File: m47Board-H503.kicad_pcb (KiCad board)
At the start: 4 copper layers, 40 x 34 mm, 42 parts, among them J1 USB_C_Receptacle_USB2.0_16P, J3 Conn_01x15_Pin, J4 Conn_01x10_Pin, J5 Conn_01x15_Pin, SW1 SW_Push, SW2 SW_Push, SW3 SW_Push, U1 AP2114H-3.3TRG1, U2 STM32H503CBTx, U3 USBLC6-2SC6, Y1 CX3225FB16000F0FZZH1 16MHz, Y2 ABS07-32.768KHZ-T

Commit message: Route tracks
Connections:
- J3 pad 14: Net-(J3-Pin_14) -> GND
- J3 pad 15: Net-(J3-Pin_15) -> +3.3V
- J4 pad 1: unconnected-(J4-Pin_1-Pad1) -> Net-(J4-Pin_1)
- J4 pad 10: unconnected-(J4-Pin_10-Pad10) -> /PA7
- J4 pad 2: unconnected-(J4-Pin_2-Pad2) -> Net-(J4-Pin_2)
- J4 pad 3: unconnected-(J4-Pin_3-Pad3) -> /PA0
- J4 pad 4: unconnected-(J4-Pin_4-Pad4) -> /PA1
- J4 pad 5: unconnected-(J4-Pin_5-Pad5) -> /PA2
- J4 pad 6: unconnected-(J4-Pin_6-Pad6) -> /PA3
- J4 pad 7: unconnected-(J4-Pin_7-Pad7) -> /PA4
- J4 pad 8: unconnected-(J4-Pin_8-Pad8) -> /PA5
- J4 pad 9: unconnected-(J4-Pin_9-Pad9) -> /PA6
- J5 pad 1: unconnected-(J5-Pin_1-Pad1) -> +3.3V
- J5 pad 10: unconnected-(J5-Pin_10-Pad10) -> /PB15
- J5 pad 11: unconnected-(J5-Pin_11-Pad11) -> /PA8
- J5 pad 12: unconnected-(J5-Pin_12-Pad12) -> /PA9
- J5 pad 13: unconnected-(J5-Pin_13-Pad13) -> /PA10
- J5 pad 14: unconnected-(J5-Pin_14-Pad14) -> GND
- J5 pad 15: unconnected-(J5-Pin_15-Pad15) -> VBUS
- J5 pad 2: unconnected-(J5-Pin_2-Pad2) -> GND
- J5 pad 3: unconnected-(J5-Pin_3-Pad3) -> /PB0
- J5 pad 4: unconnected-(J5-Pin_4-Pad4) -> /PB1
- J5 pad 5: unconnected-(J5-Pin_5-Pad5) -> /PB2
- J5 pad 6: unconnected-(J5-Pin_6-Pad6) -> /PB10
- J5 pad 7: unconnected-(J5-Pin_7-Pad7) -> /PB12
- J5 pad 8: unconnected-(J5-Pin_8-Pad8) -> /PB13
- J5 pad 9: unconnected-(J5-Pin_9-Pad9) -> /PB14
- R6 pad 2: Net-(J3-Pin_14) -> Net-(J4-Pin_1)
- R7 pad 2: Net-(J3-Pin_15) -> Net-(J4-Pin_2)
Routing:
- net GND: track 18.4 -> 57.9 mm, vias 9 -> 33
- net /PC13: track 32.0 -> 60.4 mm, vias 1 -> 2
- net /PA7: track 0.00 -> 23.4 mm, vias 0 -> 1
- net /PB0: track 0.00 -> 23.2 mm, vias 0 -> 1
- net /PA6: track 0.00 -> 22.6 mm, vias 0 -> 1
- net /PA10: track 0.00 -> 22.4 mm, vias 0 -> 1
- net /PA0: track 0.00 -> 21.5 mm, vias 0 -> 1
- net /PB1: track 0.00 -> 20.4 mm, vias 0 -> 1
- net /PA4: track 0.00 -> 19.8 mm, vias 0 -> 1
- net /PB2: track 0.00 -> 19.8 mm, vias 0 -> 1
- net /PA1: track 0.00 -> 19.7 mm, vias 0 -> 1
- net /PA5: track 2.12 -> 21.8 mm, vias 0 -> 1
- net /PA9: track 0.00 -> 18.8 mm, vias 0 -> 1
- net /PA3: track 0.00 -> 18.5 mm, vias 0 -> 1
- net /PA8: track 0.00 -> 18.3 mm, vias 0 -> 1
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
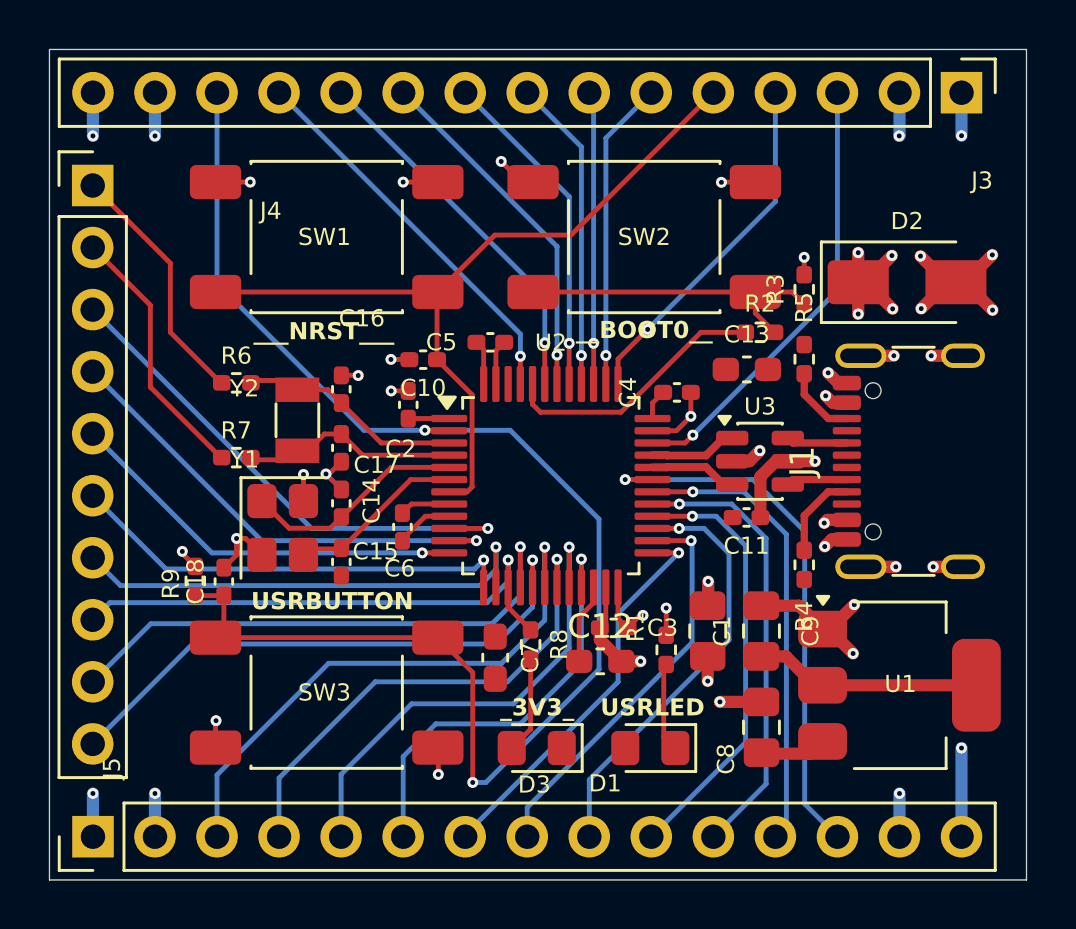
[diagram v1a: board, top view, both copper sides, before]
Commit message: Route trakcs, arrange silkscreen
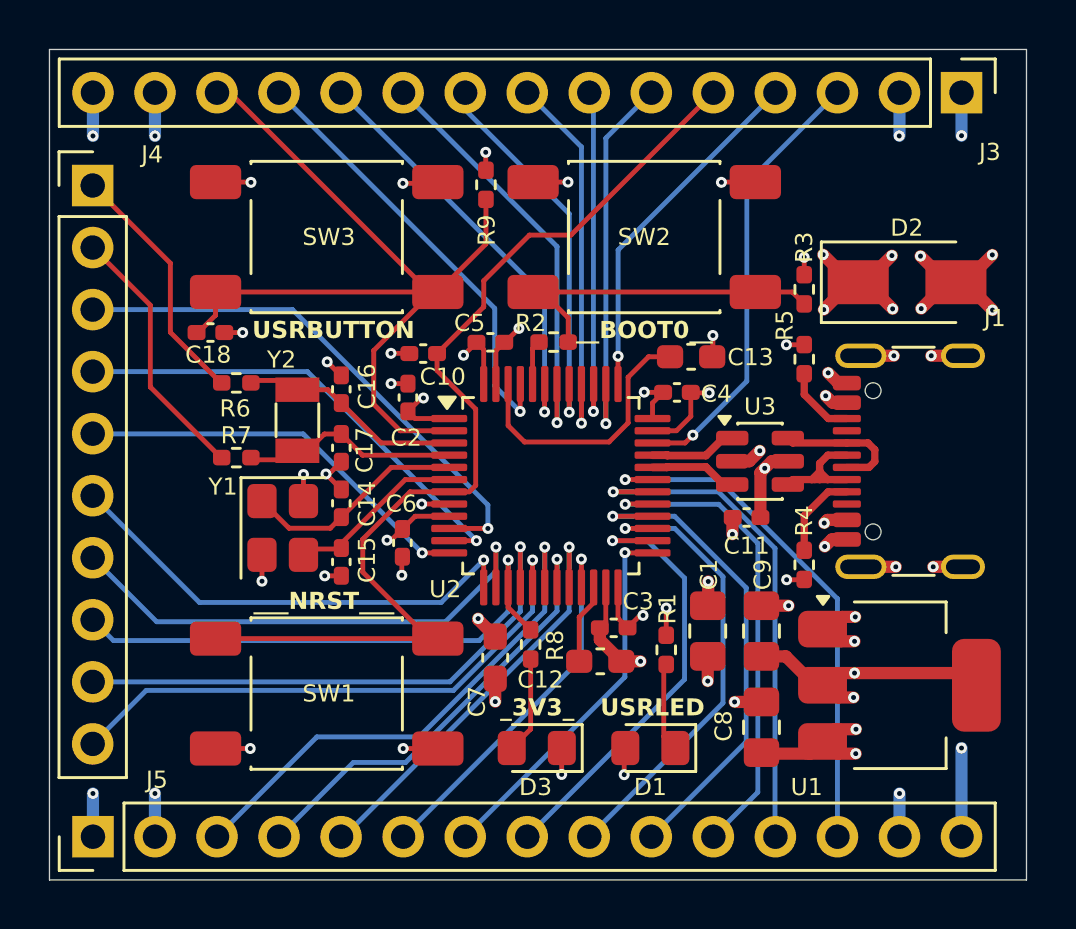
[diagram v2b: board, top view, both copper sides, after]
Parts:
- moved R9 20.1 mm to (137.9, 91.5)
- moved SW1 18.7 mm to (131.3, 112.4), turned to 180 degrees
- moved SW3 18.6 mm to (131.3, 93.7), turned to 180 degrees
- moved C18 10.2 mm to (126.6, 97.6), turned to 0 degrees
- moved R2 8.46 mm to (140.6, 98.0)
- moved C13 2.34 mm to (146.3, 98.6)
- moved C6 0.65 mm to (134.4, 106.2), turned to -90 degrees
- moved C2 0.30 mm to (134.7, 100.2)
- moved C10 0.25 mm to (135.3, 98.5)
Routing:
- net /PC13: track 60.4 -> 37.9 mm, vias 2 -> 0
- net Net-(C13-Pad1): track 0.00 -> 11.1 mm
- net /NRST: track 33.4 -> 43.1 mm
- net /BOOT0: track 11.0 -> 1.83 mm
- net +3.3V: track 29.3 -> 36.8 mm, vias 8 -> 16
- net GND: track 57.9 -> 62.3 mm, vias 33 -> 45
- net VBUS: track 19.1 -> 22.5 mm, vias 8 -> 10
- net /PA15: track 12.7 -> 15.9 mm
- net /PB4: track 12.8 -> 16.1 mm
- net /PB6: track 14.5 -> 17.7 mm
- net Net-(J1-D+-PadA6): track 2.56 -> 5.55 mm
- net Net-(J1-D--PadA7): track 2.50 -> 5.45 mm
- net /PB2: track 19.8 -> 17.4 mm
- net /PB5: track 13.7 -> 16.0 mm
- net /PB15: track 17.8 -> 20.1 mm
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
